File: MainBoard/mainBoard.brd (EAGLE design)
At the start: 99 x 99.2 mm, 150 parts, among them IC1 74HC151D, IC2 LM317, IC3 74HC238, IC4 FT232RL, J1 22-05-7038-03, J10 22-05-7038-03, J11 22-05-7038-03, J12 22-05-7038-03, J13 22-05-7038-03, J14 22-05-7038-03, J15 22-05-7038-03, J16 22-05-7038-03, J19 J5MM, J2 22-05-7038-03, J3 22-05-7038-03, J4 22-05-7038-03, J5 22-05-7038-03, J6 22-05-7038-03, J7 22-05-7038-03, J8 22-05-7038-03, J9 22-05-7038-03, Q1 8MHz, Q10 BC847ASMD, Q12 BC847ASMD, Q2 BC847ASMD, Q4 BC847ASMD, Q6 BC847ASMD, Q8 BC847ASMD, X1 PWR12, X10 MSTBA2, X11 MSTBA2, X12 MSTBA2, X13 MSTBA2, X15 MINI-USB-SCHIELD-32005-301, X2 MSTBA2, X3 MSTBA2, X4 MSTBA2, X5 MSTBA2, X6 MSTBA2, X7 MSTBA2, X8 MSTBA2, X9 MSTBA2

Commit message: mainboard updates
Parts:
- removed J19: J5MM, jumper:05
- moved U$19 158.4 mm to (114.0, 70.4)
- moved U$18 156.1 mm to (113.9, 68.6)
- moved U$10 144.4 mm to (114.3, 65.0)
- moved U$9 142.7 mm to (114.2, 63.2)
- moved U$8 140.9 mm to (114.2, 61.5)
- moved U$7 139.2 mm to (114.1, 59.7)
- moved U$6 137.5 mm to (114.1, 57.9)
- moved U$5 135.7 mm to (114.0, 56.1)
- moved U$4 134.0 mm to (114.0, 54.4)
- moved U$3 132.4 mm to (113.9, 52.6)
- moved U$17 72.1 mm to (49.6, -10.2)
- moved U$16 71.3 mm to (49.6, -11.9)
- moved U$15 70.6 mm to (49.5, -13.7)
- moved U$11 62.7 mm to (-8.13, 62.3), turned to 90 degrees
- moved U$14 58.2 mm to (38.5, -10.2)
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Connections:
- net +3V3: no longer J19.1, J19.2
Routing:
- net +3V3: track 270.5 -> 276.0 mm, vias 6 -> 7
- net PA8: track 56.6 -> 58.3 mm
- net USART1_TX: track 55.0 -> 53.4 mm
- net USART1_RX: track 52.4 -> 50.8 mm
- net D_ENABLE: track 36.8 -> 35.3 mm
- net FREQ: track 30.0 -> 28.7 mm
- net PB0: track 30.9 -> 29.7 mm
- net SWDIO: track 35.1 -> 36.1 mm
- net D_RW: track 33.5 -> 32.6 mm
- net PB10: track 39.5 -> 40.1 mm
- net PA4: track 48.7 -> 49.3 mm
- net GND: vias 48 -> 49

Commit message: mainboard updates
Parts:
- moved U$12 22.2 mm to (60.5, -11.9)
- moved U$15 11.7 mm to (60.7, -10.2)
- moved X1 7.87 mm to (6.86, 64.5)
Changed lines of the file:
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@@
 <text x="93.472" y="80.01" size="1.6764" layer="25" ratio="16" rot="SR180">BT1         BT2          BT3          BT4</text>
 <text x="33.274" y="81.788" size="1.016" layer="25" ratio="16" rot="SR180">-        +</text>
-<text x="1.27" y="61.722" size="1.27" layer="25" ratio="16" rot="SR270">GND 12VDC</text>
+<text x="1.27" y="69.342" size="1.27" layer="25" ratio="16" rot="SR270">GND 12VDC</text>
 <text x="1.778" y="40.386" size="1.6764" layer="25" ratio="16">ESP8266</text>
 <text x="16.51" y="13.208" size="2.54" layer="25" ratio="16">M1</text>
@@
 <attribute name="R" value="MPE 094-2-008" x="6.604" y="44.958" size="1.778" layer="27" display="off"/>
 </element>
-<element name="X1" library="con-ptr500" package="AK500/2" value="PWR12" x="6.858" y="56.642" smashed="yes" rot="R90">
-<attribute name="OC_NEWARK" value="unknown" x="6.858" y="56.642" size="1.778" layer="27" rot="R90" display="off"/>
-<attribute name="MPN" value="" x="6.858" y="56.642" size="1.778" layer="27" rot="R90" display="off"/>
-<attribute name="MF" value="" x="6.858" y="56.642" size="1.778" layer="27" rot="R90" display="off"/>
-<attribute name="OC_FARNELL" value="unknown" x="6.858" y="56.642" size="1.778" layer="27" rot="R90" display="off"/>
-<attribute name="R" value="AKL 101-02" x="6.858" y="56.642" size="1.778" layer="27" rot="R90" display="off"/>
+<element name="X1" library="con-ptr500" package="AK500/2" value="PWR12" x="6.858" y="64.516" smashed="yes" rot="R90">
+<attribute name="OC_NEWARK" value="unknown" x="6.858" y="64.516" size="1.778" layer="27" rot="R90" display="off"/>
+<attribute name="MPN" value="" x="6.858" y="64.516" size="1.778" layer="27" rot="R90" display="off"/>
+<attribute name="MF" value="" x="6.858" y="64.516" size="1.778" layer="27" rot="R90" display="off"/>
+<attribute name="OC_FARNELL" value="unknown" x="6.858" y="64.516" size="1.778" layer="27" rot="R90" display="off"/>
+<attribute name="R" value="AKL 101-02" x="6.858" y="64.516" size="1.778" layer="27" rot="R90" display="off"/>
 </element>
 <element name="Q2" library="transistor-npn" package="SOT23" value="BC847ASMD" x="18.542" y="24.384" smashed="yes" rot="R180">
@@
 <element name="U$10" library="extra" package="DUMMY_BOM" value="PSK 254/3W" x="114.28289375" y="65.024"/>
 <element name="U$11" library="extra" package="DUMMY_BOM" value="EA DOGM204W-A" x="-8.128" y="62.2647875" rot="R90"/>
-<element name="U$12" library="extra" package="DUMMY_BOM" value="AKL 249-02" x="38.44068125" y="-13.716"/>
+<element name="U$12" library="extra" package="DUMMY_BOM" value="AKL 249-02" x="60.53868125" y="-11.938"/>
 <element name="U$13" library="extra" package="DUMMY_BOM" value="AKL 249-02" x="38.492575" y="-11.938"/>
 <element name="U$14" library="extra" package="DUMMY_BOM" value="AKL 249-02" x="38.54446875" y="-10.16"/>
-<element name="U$15" library="extra" package="DUMMY_BOM" value="AKL 249-02" x="49.5183625" y="-13.716"/>
+<element name="U$15" library="extra" package="DUMMY_BOM" value="AKL 249-02" x="60.6943625" y="-10.16"/>
 <element name="U$16" library="extra" package="DUMMY_BOM" value="AKL 249-02" x="49.57025625" y="-11.938"/>
 <element name="U$17" library="extra" package="DUMMY_BOM" value="AKL 249-02" x="49.62215" y="-10.16"/>
@@
 <wire x1="16.19" y1="95.504" x2="16.19" y2="93.372" width="0.6096" layer="1"/>
 <wire x1="16.19" y1="93.372" x2="16.496" y2="93.066" width="0.6096" layer="1"/>
-<wire x1="8.636" y1="20.4802125" x2="8.636" y2="27.94" width="1.778" layer="1"/>
-<wire x1="8.636" y1="27.94" x2="8.636" y2="28.286946875" width="1.778" layer="1"/>
-<wire x1="13.462" y1="35.7202125" x2="13.462" y2="47.0837875" width="1.778" layer="1"/>
-<wire x1="13.462" y1="47.0837875" x2="13.16910625" y2="47.79089375" width="1.778" layer="1" curve="45"/>
-<wire x1="13.16910625" y1="47.79089375" x2="6.858" y2="54.102" width="1.778" layer="1"/>
+<wire x1="8.636" y1="20.4802125" x2="8.636" y2="30.0657875" width="1.778" layer="1"/>
+<wire x1="13.462" y1="46.99" x2="13.462" y2="35.7202125" width="1.778" layer="1"/>
+<wire x1="13.462" y1="35.7202125" x2="13.16910625" y2="35.01310625" width="1.778" layer="1" curve="-45"/>
+<wire x1="13.16910625" y1="35.01310625" x2="8.92889375" y2="30.77289375" width="1.778" layer="1"/>
 <contactref element="Q13" pad="1"/>
 <contactref element="Q13" pad="3"/>
@@
 <contactref element="C17" pad="1"/>
 <contactref element="R28" pad="2"/>
+<wire x1="13.462" y1="46.99" x2="13.462" y2="47.0837875" width="1.778" layer="1"/>
 <wire x1="71.816" y1="25.654" x2="71.816" y2="23.114" width="0.6096" layer="1"/>
 <wire x1="71.816" y1="23.114" x2="72.009" y2="22.921" width="0.6096" layer="1"/>
@@
 <vertex x="70.739" y="17.653"/>
 </polygon>
-<wire x1="6.858" y1="54.102" x2="8.9837875" y2="54.102" width="1.27" layer="1"/>
-<wire x1="8.9837875" y1="54.102" x2="9.69089375" y2="54.39489375" width="1.27" layer="1" curve="45"/>
-<wire x1="9.69089375" y1="54.39489375" x2="10.62910625" y2="55.33310625" width="1.27" layer="1"/>
-<wire x1="10.62910625" y1="55.33310625" x2="10.922" y2="56.0402125" width="1.27" layer="1" curve="45"/>
-<wire x1="10.922" y1="56.0402125" x2="10.922" y2="87.0777875" width="1.27" layer="1"/>
+<wire x1="10.922" y1="87.0777875" x2="10.922" y2="63.9142125" width="1.27" layer="1"/>
+<wire x1="10.922" y1="63.9142125" x2="10.62910625" y2="63.20710625" width="1.27" layer="1" curve="-45"/>
+<wire x1="10.62910625" y1="63.20710625" x2="9.71629375" y2="62.29429375" width="1.27" layer="1"/>
 <wire x1="10.922" y1="87.0777875" x2="11.21489375" y2="87.78489375" width="1.27" layer="1" curve="-45"/>
-<wire x1="13.462" y1="35.7202125" x2="13.16910625" y2="35.01310625" width="1.778" layer="1" curve="-45"/>
-<wire x1="13.16910625" y1="35.01310625" x2="8.92889375" y2="30.77289375" width="1.778" layer="1"/>
 <wire x1="8.92889375" y1="30.77289375" x2="8.636" y2="30.0657875" width="1.778" layer="1" curve="45"/>
-<wire x1="8.636" y1="30.0657875" x2="8.636" y2="28.286946875" width="1.778" layer="1"/>
+<wire x1="9.71629375" y1="62.29429375" x2="9.0091875" y2="62.0014" width="1.27" layer="1" curve="-45"/>
+<wire x1="9.0091875" y1="62.0014" x2="6.858" y2="62.0014" width="1.27" layer="1"/>
+<wire x1="13.462" y1="46.99" x2="13.462" y2="52.4177875" width="1.778" layer="1"/>
+<wire x1="13.462" y1="52.4177875" x2="13.16910625" y2="53.12489375" width="1.778" layer="1" curve="45"/>
+<wire x1="13.16910625" y1="53.12489375" x2="7.15089375" y2="59.14310625" width="1.778" layer="1"/>
+<wire x1="7.15089375" y1="59.14310625" x2="6.858" y2="59.8502125" width="1.778" layer="1" curve="-45"/>
+<wire x1="6.858" y1="59.8502125" x2="6.858" y2="62.0014" width="1.778" layer="1"/>
 <wire x1="10.922" y1="87.0777875" x2="10.02" y2="84.074" width="0" layer="19" extent="1-1"/>
-<wire x1="6.858" y1="54.1274" x2="6.858" y2="54.102" width="0" layer="19" extent="1-1"/>
 <wire x1="10.8282125" y1="17.526" x2="8.636" y2="20.4802125" width="0" layer="19" extent="1-1"/>
 <wire x1="60.325" y1="20.126" x2="60.452" y2="17.526" width="0" layer="19" extent="1-1"/>

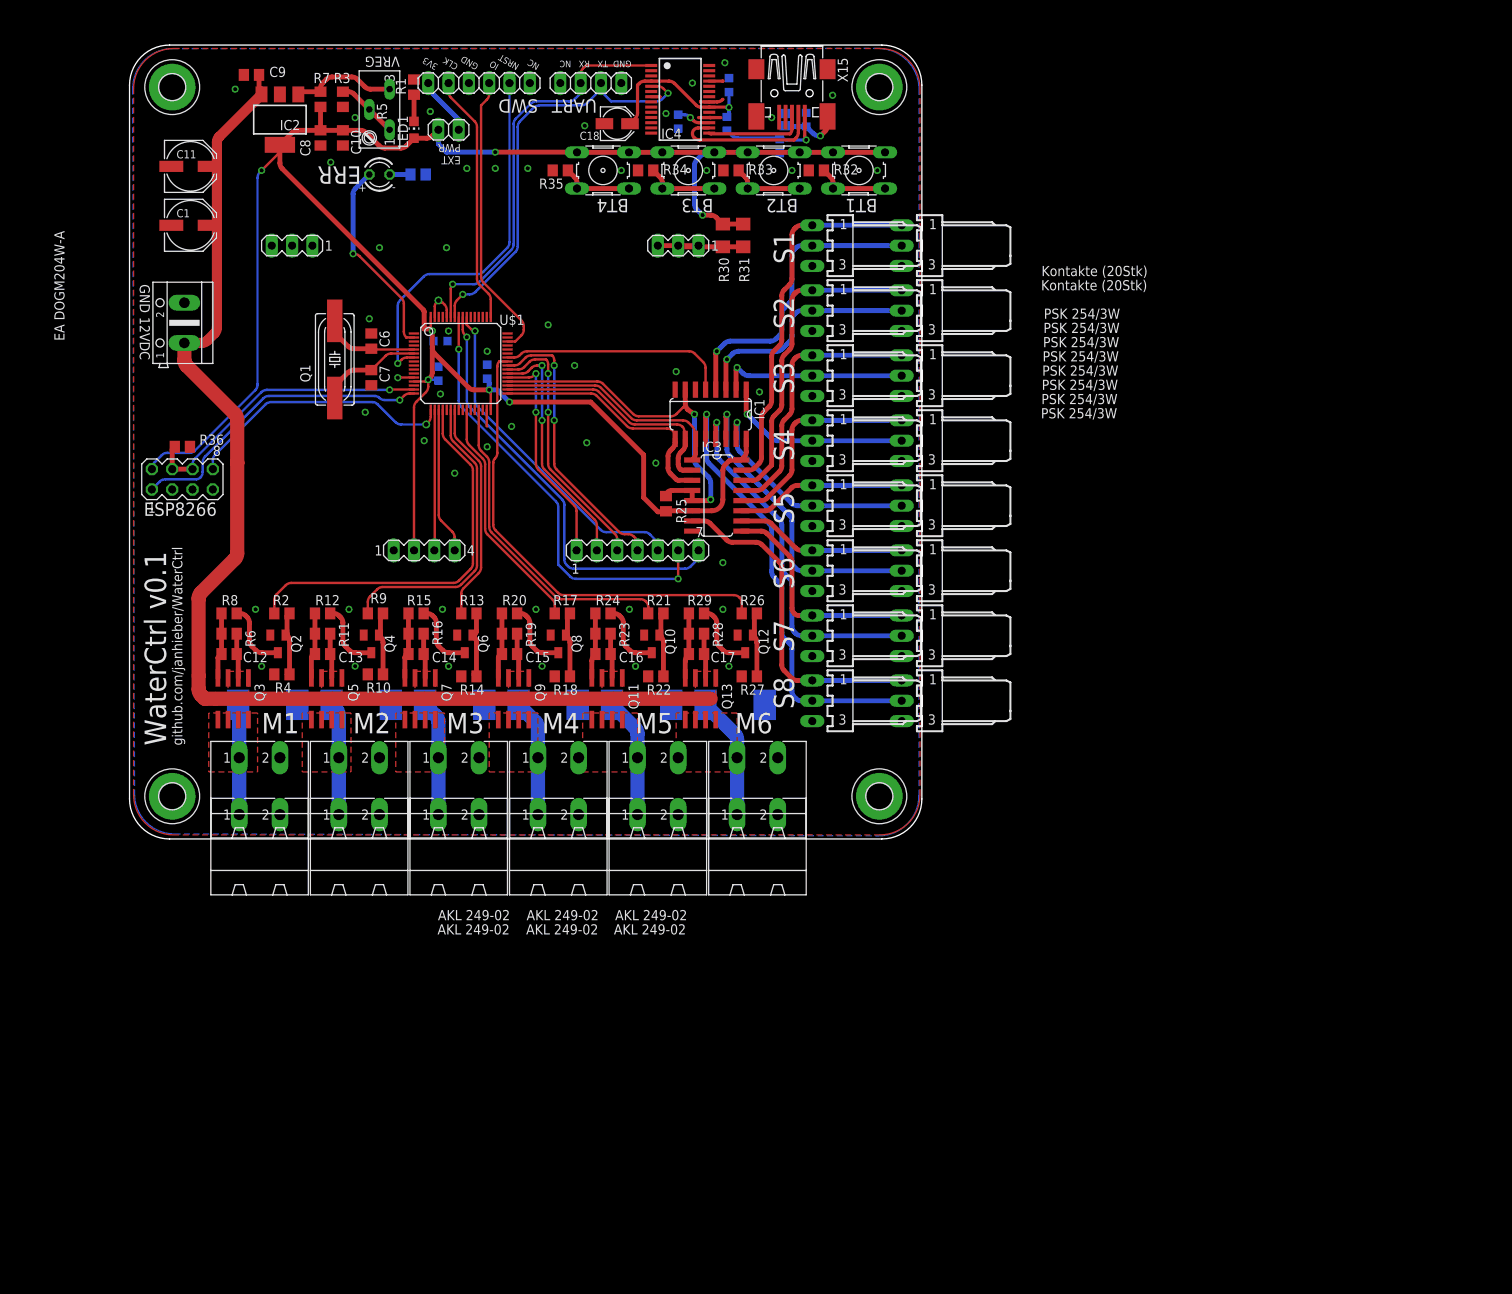
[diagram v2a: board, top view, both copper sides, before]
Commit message: mainboard redesign
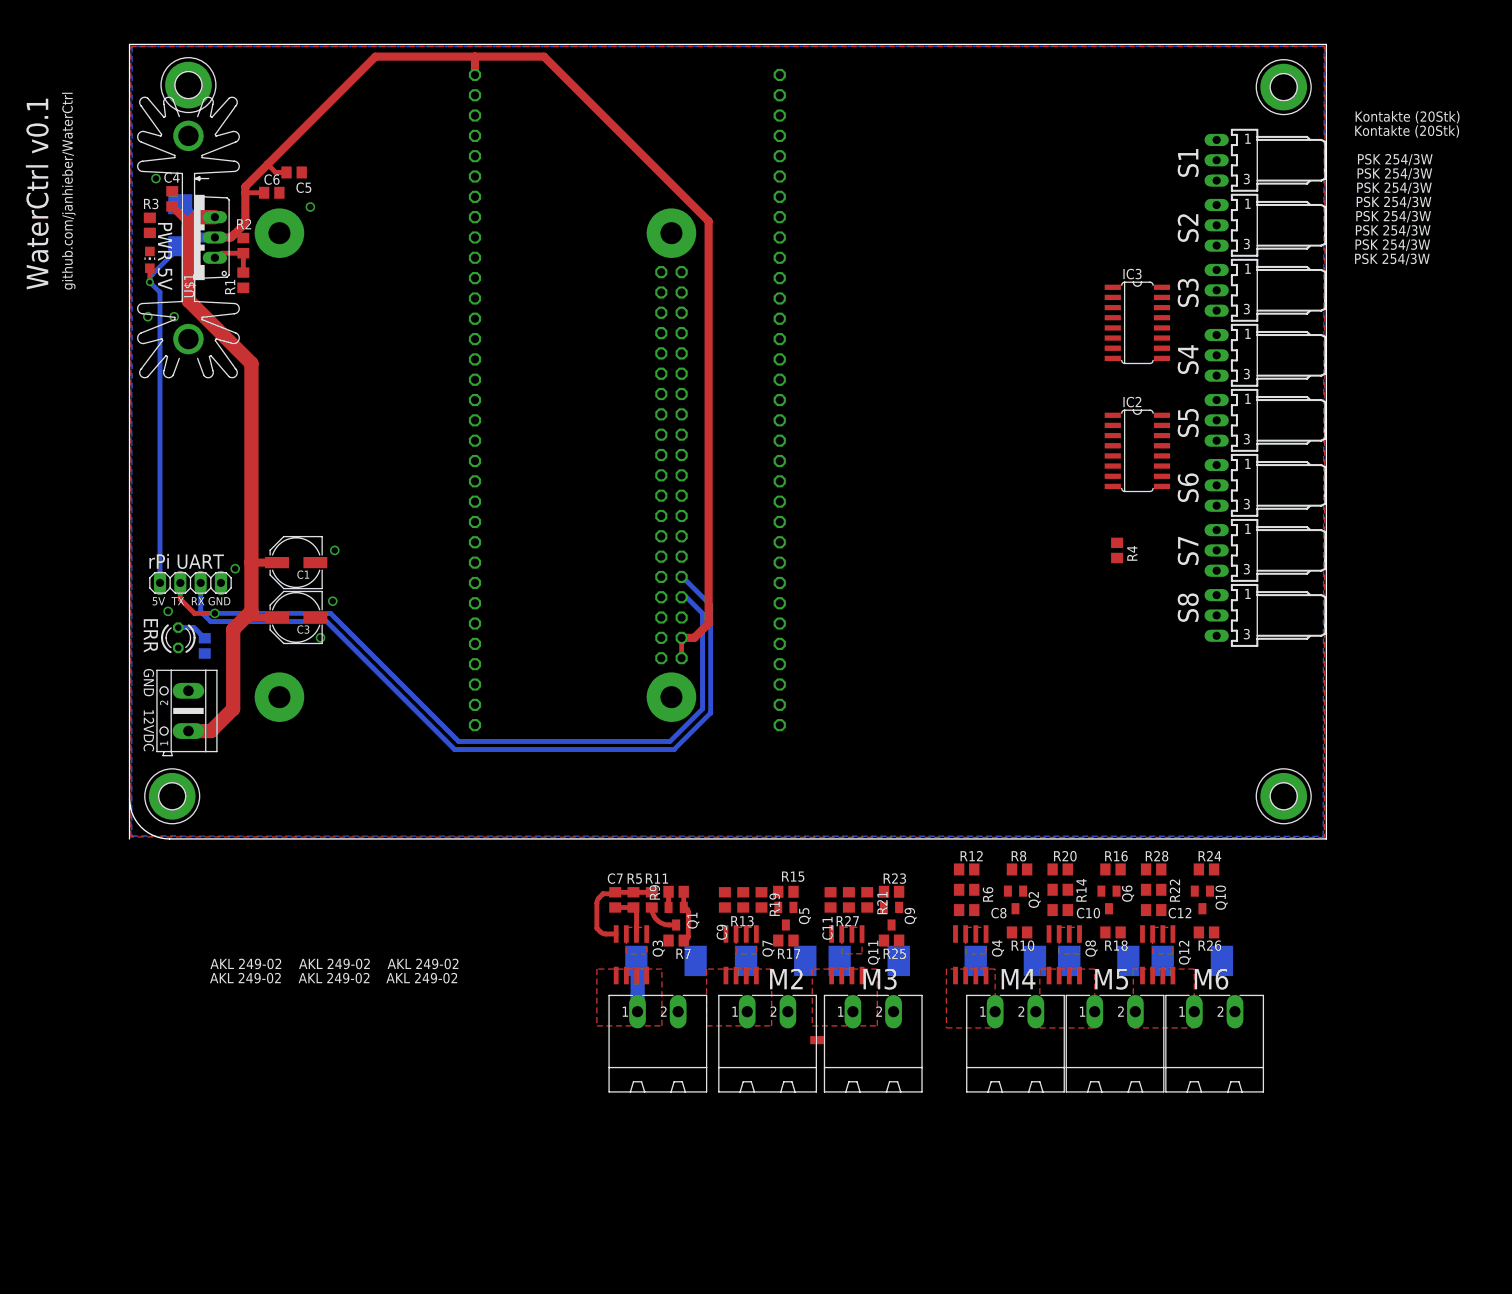
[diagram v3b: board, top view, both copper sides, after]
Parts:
- removed C13, C14, C15, C16, C17: 100n, rcl:C0805
- removed C18: 4.7u/35V, rcl:PANASONIC_B
- removed C19: 10n, rcl:C0603K
- removed C2, C20: 100n, rcl:C0603K
- removed IC1: 74HC151D, 74xx-eu:SO16
- removed IC4: FT232RL, ftdichip:SSOP28
- removed J10, J11, J12, J13, J14, J15, J16, J9: 22-05-7038-03, con-molex:7395-03
- removed JP2: EXTPWR, pinhead:1X02
- removed JP3: UART, pinhead:1X04
- removed Q13: (no value), transistor-power:SO-08
- removed R30, R31: 2R4 1/4W, rcl:R1206
- removed R32, R33, R34, R35, R36: 18k, rcl:R0805
- removed R37, R38: EMI 60Ohm Ferrit, rcl:R0603
- removed R39: 100, rcl:R0805
- removed S1, S2, S3, S4: (no value), switch-omron:B3F-10XX
- removed SJ1: (no value), jumper:SJ
- removed SV1: ESP8266, con-lstb:MA04-2
- removed SV2: DISP_A, con-lstb:MA03-1
- removed SV3: DISP_B, con-lstb:MA03-1
- removed SV4: DISP_C, con-lstb:MA04-1
- removed SV5: DISP_D, con-lstb:MA07-1
- removed U$18, U$19: Kontakte (20Stk), extra:DUMMY_BOM
- removed X10, X11, X12, X13, X8, X9: MSTBA2, con-phoenix-508:MSTBA2
- removed X15: MINI-USB-SCHIELD-32005-301, con-cypressindustries:32005-301
- added D7: (no value), diode:SMC
- added KK1: SK104-PAD, heatsink:SK104-PAD
- added PCB1: RASPBERRY_PI_B+_TPLACE, RASPBERRY_PI_Bplus:RASPBERRY_PI_BPLUS_TPLACE
- added U$2: PSK 254/3W, extra:DUMMY_BOM
- added U1: STM32F0DISCOVERY, extra:STM32F0DISCOVERY
- C10: value 1u -> 100n
- C11: value 47u/25V -> 100n; device rcl:PANASONIC_D -> rcl:C0805
- C3: value 100n -> 47u/25V; device rcl:C0603K -> rcl:PANASONIC_D
- C4, C5: device rcl:C0603K -> rcl:C0805
- C6: value 22p -> 1u
- C7: value 22p -> 100n
- D1: device diode:SMC -> diode:MELF-MLL41
- IC2: value LM317 -> 74HC238; device v-reg:SOT223 -> 74xx-eu:SO16
- IC3: value 74HC238 -> 74HC151D
- JP1: value SWD -> (none); device pinhead:1X06 -> pinhead:1X04
- Q1: value 8MHz -> BC847ASMD; device crystal:HC49UP -> transistor-npn:SOT23
- Q12, Q4, Q8: value BC847ASMD -> (none); device transistor-npn:SOT23 -> transistor-power:SO-08
- Q5, Q9: value (none) -> BC847ASMD; device transistor-power:SO-08 -> transistor-npn:SOT23
- R1: value 100 -> 750
- R11, R19, R28: value 1k2 -> 560
- R13, R21: value 10k -> 1k2
- R14, R22: value 18k -> 1k2
- R15, R23: value 1k2 -> 10k
- R16, R24, R8: value 560 -> 10k
- R17, R26, R9: value 10k -> 18k
- R2: value 10k -> 240
- R27: value 18k -> 560
- R29: value 560 -> 100
- R3: value 300 -> 100
- R5: value 200 -> 1k2; device pot:S64Y -> rcl:R0805
- R7: value 240 -> 10k
- U$1: value STM32 F051 R4T6 -> LM350; device stm32F:LQFP64 -> extra:TO220
- U$10: value PSK 254/3W -> Kontakte (20Stk)
- U$11: value EA DOGM204W-A -> Kontakte (20Stk)
- moved U$11 163.5 mm to (153.1, 89.7), turned to 0 degrees
- moved C10 131.7 mm to (116.3, -8.89), turned to 180 degrees
- moved C8 125.9 mm to (104.6, -8.89), turned to 180 degrees
- moved C11 121.7 mm to (87.6, -7.62), turned to 90 degrees
- moved C12 119.9 mm to (128.0, -8.89)
- moved C9 118.9 mm to (74.4, -7.62), turned to 90 degrees
- moved IC2 114.9 mm to (126.0, 48.5), turned to 270 degrees
- moved R7 114.2 mm to (68.3, -12.7), turned to 0 degrees
- moved R4 105.5 mm to (123.4, 36.1), turned to 270 degrees
- moved R8 103.9 mm to (111.3, -3.81), turned to 0 degrees
- moved R5 103.8 mm to (63.0, -7.62)
- moved Q2 97.6 mm to (110.7, -7.62)
- moved R6 97.6 mm to (104.6, -6.35)
- moved R16 92.8 mm to (122.9, -3.81), turned to 0 degrees
- moved R10 86.7 mm to (111.3, -11.7)
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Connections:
- removed net +12V: C1.+, C11.+, C12.1, C13.1, C14.1, C15.1, C16.1, C17.1, C9.1, IC2.3, Q11.1, Q11.2, Q11.3, Q13.1, Q13.2, Q13.3, Q3.1, Q3.2, Q3.3, Q5.1, Q5.2, Q5.3, Q7.1, Q7.2, Q7.3, Q9.1, Q9.2, Q9.3, R11.2, R15.2, R19.2, R23.2, R28.2, R6.2, X1.1
- removed net DM: IC4.16, X15.2
- removed net DP: IC4.15, X15.3
- removed net D_ENABLE: SV5.4, U$1.40
- removed net D_IM1: SV4.3, U$1.18
- removed net D_IM2: SV4.4, U$1.19
- removed net D_RESET: SV5.1, U$1.37
- removed net D_RS: SV5.2, U$1.38
- removed net D_RW: SV5.3, U$1.39
- removed net ID: X15.4
- removed net N$1: JP1.1, JP2.2
- removed net N$12: R3.1, R5.A, R5.S
- removed net N$23: R30.1, R31.1, SV2.1, SV2.2, SV2.3
- removed net N$24: U$1.44
- removed net N$25: U$1.45
- removed net N$27: R38.2, SJ1.2, X15.M3
- removed net N$32: C20.1, IC4.17
- removed net NRST: JP1.5, U$1.7
- removed net OSC_IN: C6.1, Q1.1, U$1.5
- removed net OSC_OUT: C7.1, Q1.2, U$1.6
- removed net PA10: U$1.43
- removed net PA5: U$1.21
- removed net SPI1_MISO: SV5.7, U$1.56
- removed net SPI1_MOSI: SV5.6, U$1.57
- removed net SPI1_SCK: SV5.5, U$1.55
- removed net SW1: R32.2, S1.3, S1.4
- removed net SW2: R33.2, S2.3, S2.4
- removed net SW3: R34.2, S3.3, S3.4
- removed net SW4: R35.2, S4.3, S4.4
- removed net SWCLK: JP1.2, U$1.49
- removed net SWDIO: JP1.4, U$1.46
- removed net USART1_RX: IC4.1, JP3.2, U$1.59
- removed net USART1_TX: IC4.5, JP3.3, U$1.58
- removed net USART2_RX: SV1.8, U$1.17
- removed net USART2_TX: SV1.1, U$1.16
- removed net VBAT: U$1.1
- removed net VBUS: C19.1, R37.1, X15.1
- removed net VCCUSB: C18.+, C2.1, IC4.20, IC4.4, R37.2
- removed net WIFI_RESET: R36.2, SV1.4, SV1.6, U$1.15
- new net +15V: C1.+, C10.1, C11.1, C12.1, C3.+, C4.1, C7.1, C8.1, C9.1, D1.C, Q11.1, Q11.2, Q11.3, Q12.1, Q12.2, Q12.3, Q3.1, Q3.2, Q3.3, Q4.1, Q4.2, Q4.3, Q7.1, Q7.2, Q7.3, Q8.1, Q8.2, Q8.3, R13.2, R14.2, R21.2, R22.2, R5.2, R6.2, U$1.3, X1.1
- new net +5V: C5.1, C6.1, D1.A, IC2.16, IC2.6, IC3.16, JP1.1, LED1.A, PCB1.2, PCB1.4, R2.2, U$1.2, U1.66
- new net 3V3: PCB1.1, PCB1.17
- new net RPI_RXD: JP1.3, PCB1.10
- new net RPI_TXD: JP1.2, PCB1.8
- net +3V3: now also R4.2, U1.1; no longer C10.1, C3.1, C4.1, C5.1, C8.1, IC1.16, IC2.4, IC3.16, IC3.6, JP2.1, LED1.A, R25.2, R30.2, R31.2, R7.2, S1.1, S1.2, S2.1, S2.2, S3.1, S3.2, S4.1, S4.2, SV1.2, SV4.2, U$1.13, U$1.32, U$1.64
- net ERROR_LED: no longer U$1.2
- net FREQ: now also IC3.5; no longer IC1.5, U$1.42
- net GND: now also C3.-, D7.A, IC2.8, JP1.4, PCB1.14, PCB1.20, PCB1.25, PCB1.30, PCB1.34, PCB1.39, PCB1.6, PCB1.9, Q1.2, Q5.2, Q9.2, R1.2, R17.1, R25.1, R26.1, R29.1, R3.1, R9.1, U1.2, U1.33, U1.34, U1.65, U1.9; no longer C10.2, C11.-, C18.-, C19.2, C2.2, C20.2, C3.2, C7.2, C8.2, C9.2, D1.A, IC1.8, IC4.18, IC4.21, IC4.25, IC4.7, J10.3, J11.3, J12.3, J13.3, J14.3, J15.3, J16.3, J9.3, JP1.3, JP3.4, Q12.2, Q4.2, Q8.2, R1.1, R14.1, R22.1, R27.1, R3.2, R32.1, R33.1, R34.1, R35.1, R36.1, R38.1, R39.1, R4.1, SJ1.1, SV1.7, SV3.1, SV3.2, SV3.3, SV4.1, U$1.12, U$1.31, U$1.60, U$1.63, X10.2, X11.2, X12.2, X13.2, X15.5, X8.2, X9.2
- net N$10: now also Q9.3, R27.1; no longer Q6.3, R16.1
- net N$11: now also Q9.1, R23.2, R25.2; no longer Q6.1, R13.2, R14.2
- net N$13: now also C8.2, Q4.4, R12.2, R6.1; no longer C15.2, Q9.4, R19.1, R20.2
- net N$14: now also Q2.3, R12.1; no longer Q8.3, R20.1
- net N$15: now also Q2.1, R10.2, R8.2; no longer Q8.1, R17.2, R18.2
- net N$16: now also C10.2, Q8.4, R14.1, R20.2; no longer C16.2, Q11.4, R23.1, R24.2
- net N$17: now also Q6.3, R20.1; no longer Q10.3, R24.1
- net N$18: now also Q6.1, R16.2, R18.2; no longer Q10.1, R21.2, R22.2
- net N$19: now also C12.2, Q12.4, R22.1, R28.2; no longer C17.2, Q13.4, R28.1, R29.2
- net N$2: now also C9.2, Q7.4, R13.1, R19.2; no longer C13.2, Q5.4, R11.1, R12.2
- net N$20: now also R1.1, R2.1, U$1.1; no longer IC2.1, R5.E, R7.1
- net N$21: now also Q10.3, R28.1; no longer Q12.3, R29.1
- net N$22: now also Q10.1, R24.2; no longer Q12.1, R27.2
- net N$29: now also R29.2; no longer R39.2
- net N$3: now also C7.2, R11.2, R5.1; no longer C12.2, R6.1, R8.2
- net N$4: now also Q1.3, R11.1; no longer Q2.3, R8.1
- net N$5: now also Q1.1, R7.2, R9.2; no longer Q2.1, R2.2, R4.2
- net N$6: now also Q5.3, R19.1; no longer Q4.3, R12.1
- net N$7: now also Q5.1, R15.2, R17.2; no longer Q4.1, R10.2, R9.2
- net N$8: now also C11.2, Q11.4, R21.1, R27.2; no longer C14.2, Q7.4, R15.1, R16.2
- net N$9: now also R3.2; no longer R1.2
- net PA4: now also R7.1; no longer R2.1, U$1.20
- net PA6: now also R15.1; no longer R9.1, U$1.22
- net PA7: now also R23.1; no longer R13.1, U$1.23
- net PA8: now also R24.1; no longer R26.1, U$1.41
- net PB0: now also R8.1; no longer R17.1, U$1.26
- net PB10: now also R16.1; no longer R21.1, U$1.29
- net S1_3V: now also IC2.15; no longer IC3.15, J9.1
- net S1_DAT: now also IC3.4; no longer IC1.4, J9.2
- net S2_3V: now also IC2.14; no longer IC3.14, J10.1
- net S2_DAT: now also IC3.3; no longer IC1.3, J10.2
- net S3_3V: now also IC2.13; no longer IC3.13, J11.1
- net S3_DAT: now also IC3.2; no longer IC1.2, J11.2
- net S4_3V: now also IC2.12; no longer IC3.12, J12.1
- net S4_DAT: now also IC3.1; no longer IC1.1, J12.2
- net S5_3V: now also IC2.11; no longer IC3.11, J13.1
- net S5_DAT: now also IC3.15; no longer IC1.15, J13.2
- net S6_3V: now also IC2.10; no longer IC3.10, J14.1
- net S6_DAT: now also IC3.14; no longer IC1.14, J14.2
- net S7_3V: now also IC2.9; no longer IC3.9, J15.1
- net S7_DAT: now also IC3.13; no longer IC1.13, J15.2
- net S8_3V: now also IC2.7; no longer IC3.7, J16.1
- net S8_DAT: now also IC3.12; no longer IC1.12, J16.2
- net SEN_ENABLE: now also IC2.4, IC2.5, IC3.7, R4.1; no longer IC1.7, IC3.4, IC3.5, R25.1, U$1.36
- net SEN_SEL0: now also IC2.1, IC3.11; no longer IC1.11, IC3.1, U$1.35
- net SEN_SEL1: now also IC2.2, IC3.10; no longer IC1.10, IC3.2, U$1.34
- net SEN_SEL2: now also IC2.3, IC3.9; no longer IC1.9, IC3.3, U$1.33
- net WP1: now also D2.C; no longer D1.C, X8.1
- net WP2: now also D4.C, Q7.5, Q7.6, Q7.7, Q7.8; no longer D2.C, Q5.5, Q5.6, Q5.7, Q5.8, X9.1
- net WP3: now also D6.C, Q11.5, Q11.6, Q11.7, Q11.8; no longer D3.C, Q7.5, Q7.6, Q7.7, Q7.8, X10.1
- net WP4: now also D3.C, Q4.5, Q4.6, Q4.7, Q4.8; no longer D4.C, Q9.5, Q9.6, Q9.7, Q9.8, X11.1
- net WP5: now also Q8.5, Q8.6, Q8.7, Q8.8; no longer Q11.5, Q11.6, Q11.7, Q11.8, X12.1
- net WP6: now also D7.C, Q12.5, Q12.6, Q12.7, Q12.8; no longer D6.C, Q13.5, Q13.6, Q13.7, Q13.8, X13.1
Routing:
- net +3V3: track 276.0 -> 0.00 mm, vias 7 -> 0
- net +5V: track 0.00 -> 198.5 mm, vias 0 -> 1
- net +12V: track 181.9 -> 0.00 mm
- net +15V: track 0.00 -> 96.0 mm
- net RPI_RXD: track 0.00 -> 94.9 mm
- net RPI_TXD: track 0.00 -> 91.8 mm, vias 0 -> 1
- net PA8: track 58.3 -> 0.00 mm
- net S8_DAT: track 56.1 -> 0.00 mm, vias 1 -> 0
- net SPI1_MOSI: track 55.2 -> 0.00 mm, vias 2 -> 0
- net SPI1_MISO: track 54.1 -> 0.00 mm, vias 1 -> 0
- net USART1_TX: track 53.4 -> 0.00 mm, vias 2 -> 0
- net USART1_RX: track 50.8 -> 0.00 mm, vias 1 -> 0
- net PA4: track 49.3 -> 0.00 mm
- net SEN_ENABLE: track 46.9 -> 0.00 mm, vias 2 -> 0
- net NRST: track 46.9 -> 0.00 mm, vias 1 -> 0
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- added copper zone on layer 1, net +15V
- removed copper zone on layer 1, net +12V
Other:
- board size 99 x 99.2 mm -> 149.6 x 99.3 mm
- board text added: "12VDC"
- board text added: "5V TX RX GND"
- board text added: "HDMI CON"
- board text added: "PWR 5V"
- board text added: "rPi UART"
- board text removed: "- +"
- board text removed: "BT1 BT2 BT3 BT4"
- board text removed: "CLK"
- board text removed: "ESP8266"
- board text removed: "EXT PWR"
- board text removed: "GND 12VDC"
- board text removed: "GND TX RX NC"
- board text removed: "IO"
- board text removed: "M1"
- board text removed: "NC"
- board text removed: "NRST"
- board text removed: "SWD"
- board text removed: "UART"
- board text removed: "VREG"
